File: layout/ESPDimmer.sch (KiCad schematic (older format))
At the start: 11 parts, among them P1 CONN_01X03, P2 Serial, P3 LED, P4 ProgMod, P5 DS18B20, Q1 Q_NMOS_GDS, U1 LD1117S33CTR, U2 ESP-12E

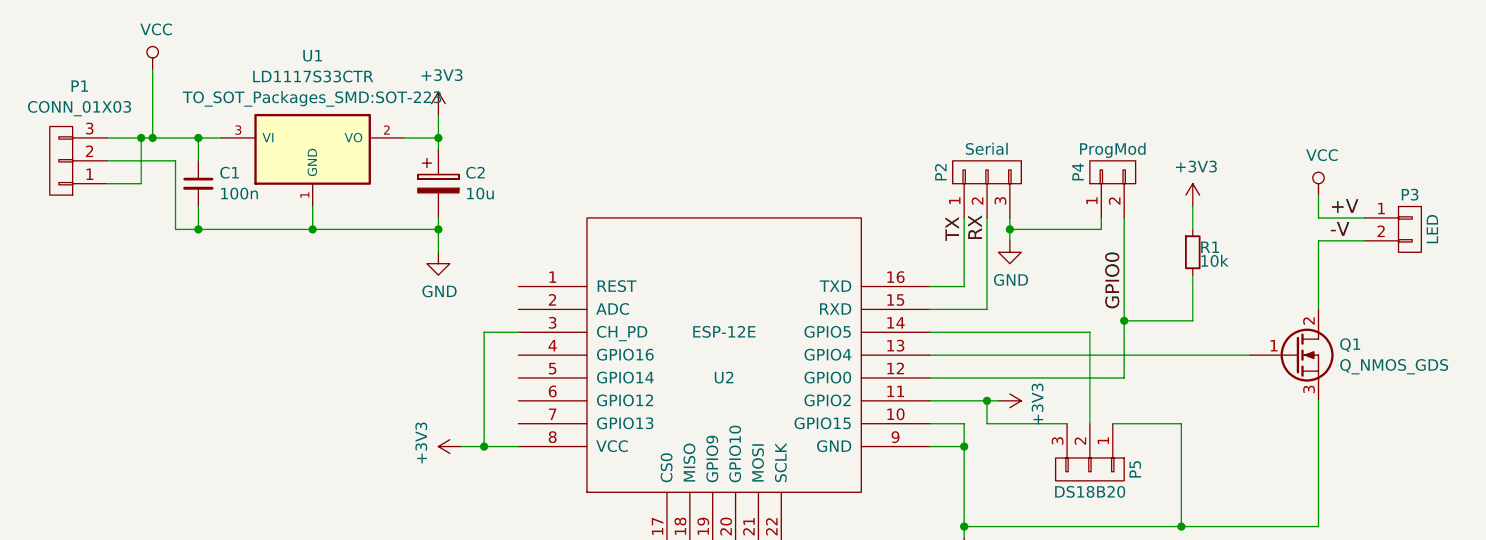
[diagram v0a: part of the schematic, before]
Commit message: Updated part names and corrected the power supply traces that were shorted!
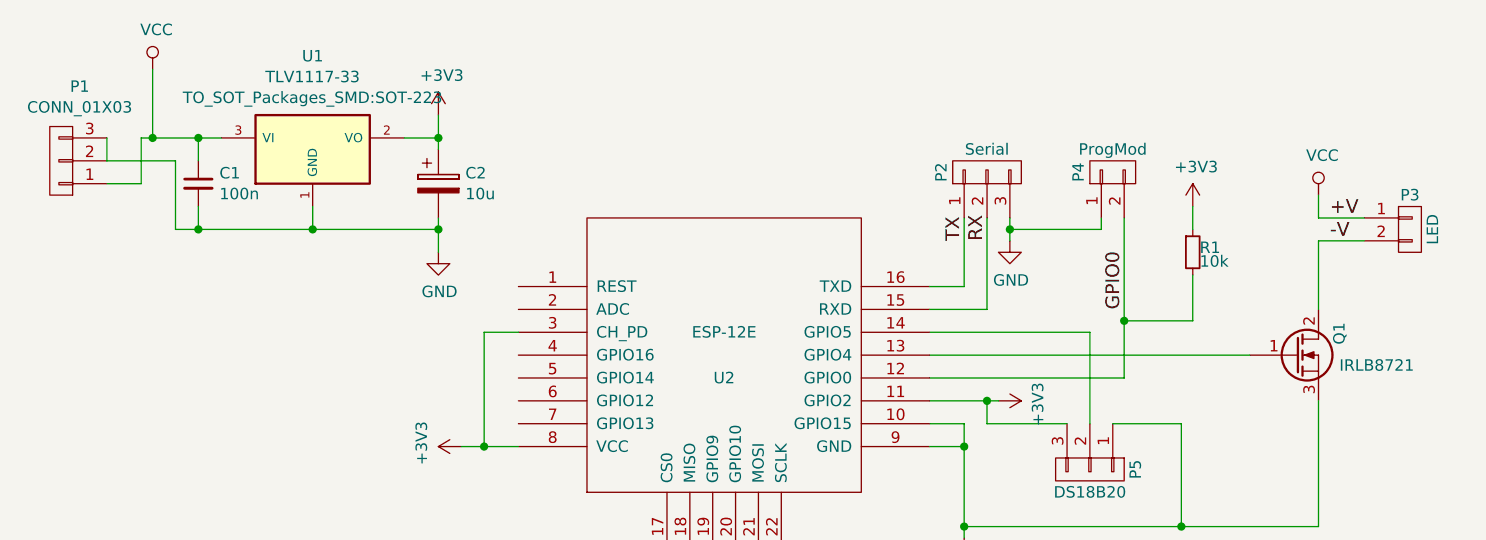
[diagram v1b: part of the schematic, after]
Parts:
- C2: footprint Capacitors_SMD:C_0402 -> Capacitors_SMD:C_0603
- Q1: value Q_NMOS_GDS -> IRLB8721
- U1: value LD1117S33CTR -> TLV1117-33
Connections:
- net GND: now also P1.3 (P3)
- net VCC: no longer P1.3 (P3)
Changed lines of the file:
@@
 P 3150 1800
 F 0 "U1" H 3150 2208 50  0000 C CNN
-F 1 "LD1117S33CTR" H 3150 2117 50  0000 C CNN
+F 1 "TLV1117-33" H 3150 2117 50  0000 C CNN
 F 2 "TO_SOT_Packages_SMD:SOT-223" H 3150 2026 50  0000 C CNN
 F 3 "" H 3150 1800 50  0000 C CNN
@@
 $EndComp
 Wire Wire Line
-	2250 1750 2750 1750
-Wire Wire Line
 	2250 1850 2550 1850
 Wire Wire Line
@@
 Wire Wire Line
 	2400 1950 2400 1750
-Connection ~ 2400 1750
 $Comp
 L CP C2
@@
 F 0 "C2" H 3818 1996 50  0000 L CNN
 F 1 "10u" H 3818 1905 50  0000 L CNN
-F 2 "Capacitors_SMD:C_0402" H 3738 1800 50  0001 C CNN
+F 2 "Capacitors_SMD:C_0603" H 3738 1800 50  0001 C CNN
 F 3 "" H 3700 1950 50  0000 C CNN
 	1    3700 1950
@@
 $EndComp
 Wire Wire Line
-	2650 1850 2650 1750
+	2650 1750 2650 1850
 Connection ~ 2650 1750
 Wire Wire Line
@@
 U 1 1 58663ECC
 P 7450 2700
-F 0 "Q1" H 7641 2746 50  0000 L CNN
-F 1 "Q_NMOS_GDS" H 7641 2655 50  0000 L CNN
+F 0 "Q1" V 7641 2746 50  0000 L CNN
+F 1 "IRLB8721" H 7641 2655 50  0000 L CNN
 F 2 "TO_SOT_Packages_THT:TO-220_Neutral123_Vertical" H 7650 2800 50  0001 C CNN
 F 3 "" H 7450 2700 50  0000 C CNN
@@
 	6100 3000 6100 2900
 Connection ~ 6100 2900
+Wire Wire Line
+	2400 1750 2750 1750
+Wire Wire Line
+	2250 1750 2250 1850
 $EndSCHEMATC

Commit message: Updated capacitors and other small changes
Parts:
- removed C2: 10u, Capacitors_SMD:C_0603, symbol CP
- added C2: 100n, Capacitors_SMD:C_0402, symbol C_Small
- added C3: 1u, Capacitors_SMD:C_0402, symbol C_Small
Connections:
- net +3V3: now also C2.1, C3.1
- net GND: now also C2.2, C3.2
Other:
- moved on the sheet: C1, P1, U1
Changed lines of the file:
@@
 L LD1117S33CTR U1
 U 1 1 57E69AF7
-P 3150 1800
-F 0 "U1" H 3150 2208 50  0000 C CNN
-F 1 "TLV1117-33" H 3150 2117 50  0000 C CNN
-F 2 "TO_SOT_Packages_SMD:SOT-223" H 3150 2026 50  0000 C CNN
-F 3 "" H 3150 1800 50  0000 C CNN
-	1    3150 1800
+P 3100 6200
+F 0 "U1" H 3100 6608 50  0000 C CNN
+F 1 "TLV1117-33" H 3100 6517 50  0000 C CNN
+F 2 "TO_SOT_Packages_SMD:SOT-223" H 3100 6426 50  0000 C CNN
+F 3 "" H 3100 6200 50  0000 C CNN
+	1    3100 6200
 	1    0    0    -1
 $EndComp
@@
 L CONN_01X03 P1
 U 1 1 57E69B46
-P 2050 1850
-F 0 "P1" H 1969 1525 50  0000 C CNN
-F 1 "CONN_01X03" H 1969 1616 50  0000 C CNN
-F 2 "Connect:BARREL_JACK" H 2050 1850 50  0001 C CNN
-F 3 "" H 2050 1850 50  0000 C CNN
-	1    2050 1850
+P 2000 6250
+F 0 "P1" H 1919 5925 50  0000 C CNN
+F 1 "CONN_01X03" H 1919 6016 50  0000 C CNN
+F 2 "Connect:BARREL_JACK" H 2000 6250 50  0001 C CNN
+F 3 "" H 2000 6250 50  0000 C CNN
+	1    2000 6250
 	-1   0    0    1
 $EndComp
 Wire Wire Line
-	2250 1850 2550 1850
-Wire Wire Line
-	2550 1850 2550 2150
-Wire Wire Line
-	2550 2150 3700 2150
-Wire Wire Line
-	3150 2150 3150 2050
-Wire Wire Line
-	2250 1950 2400 1950
-Wire Wire Line
-	2400 1950 2400 1750
-$Comp
-L CP C2
-U 1 1 57E69BD2
-P 3700 1950
-F 0 "C2" H 3818 1996 50  0000 L CNN
-F 1 "10u" H 3818 1905 50  0000 L CNN
-F 2 "Capacitors_SMD:C_0603" H 3738 1800 50  0001 C CNN
-F 3 "" H 3700 1950 50  0000 C CNN
-	1    3700 1950
-	1    0    0    -1
-$EndComp
+	2200 6250 2500 6250
+Wire Wire Line
+	2500 6250 2500 6550
+Wire Wire Line
+	2500 6550 3900 6550
+Wire Wire Line
+	3100 6550 3100 6450
+Wire Wire Line
+	2200 6350 2350 6350
+Wire Wire Line
+	2350 6350 2350 6150
 $Comp
 L C_Small C1
 U 1 1 57E69BFC
-P 2650 1950
-F 0 "C1" H 2742 1996 50  0000 L CNN
-F 1 "100n" H 2742 1905 50  0000 L CNN
-F 2 "Capacitors_SMD:C_0402" H 2650 1950 50  0001 C CNN
-F 3 "" H 2650 1950 50  0000 C CNN
-	1    2650 1950
-	1    0    0    -1
-$EndComp
-Wire Wire Line
-	2650 1750 2650 1850
-Connection ~ 2650 1750
-Wire Wire Line
-	2650 2050 2650 2150
-Connection ~ 2650 2150
-Wire Wire Line
-	3700 2100 3700 2250
-Connection ~ 3150 2150
-Wire Wire Line
-	3550 1750 3700 1750
-Wire Wire Line
-	3700 1650 3700 1800
+P 2600 6350
+F 0 "C1" H 2692 6396 50  0000 L CNN
+F 1 "100n" H 2692 6305 50  0000 L CNN
+F 2 "Capacitors_SMD:C_0402" H 2600 6350 50  0001 C CNN
+F 3 "" H 2600 6350 50  0000 C CNN
+	1    2600 6350
+	1    0    0    -1
+$EndComp
+Wire Wire Line
+	2600 6150 2600 6250
+Connection ~ 2600 6150
+Wire Wire Line
+	2600 6450 2600 6550
+Connection ~ 2600 6550
+Wire Wire Line
+	3650 6400 3650 6650
+Connection ~ 3100 6550
+Wire Wire Line
+	3500 6150 3900 6150
+Wire Wire Line
+	3650 6050 3650 6200
 $Comp
 L GND #PWR01
 U 1 1 57E69D04
-P 3700 2250
-F 0 "#PWR01" H 3700 2000 50  0001 C CNN
-F 1 "GND" H 3705 2077 50  0000 C CNN
-F 2 "" H 3700 2250 50  0000 C CNN
-F 3 "" H 3700 2250 50  0000 C CNN
-	1    3700 2250
-	1    0    0    -1
-$EndComp
-Connection ~ 3700 1750
-Connection ~ 3700 2150
+P 3650 6650
+F 0 "#PWR01" H 3650 6400 50  0001 C CNN
+F 1 "GND" H 3655 6477 50  0000 C CNN
+F 2 "" H 3650 6650 50  0000 C CNN
+F 3 "" H 3650 6650 50  0000 C CNN
+	1    3650 6650
+	1    0    0    -1
+$EndComp
+Connection ~ 3650 6150
+Connection ~ 3650 6550
 $Comp
 L GND #PWR02
@@
 L +3V3 #PWR03
 U 1 1 586638C3
-P 3700 1650
-F 0 "#PWR03" H 3700 1500 50  0001 C CNN
-F 1 "+3V3" H 3715 1823 50  0000 C CNN
-F 2 "" H 3700 1650 50  0000 C CNN
-F 3 "" H 3700 1650 50  0000 C CNN
-	1    3700 1650
+P 3650 6050
+F 0 "#PWR03" H 3650 5900 50  0001 C CNN
+F 1 "+3V3" H 3665 6223 50  0000 C CNN
+F 2 "" H 3650 6050 50  0000 C CNN
+F 3 "" H 3650 6050 50  0000 C CNN
+	1    3650 6050
 	1    0    0    -1
 $EndComp
@@
 L VCC #PWR04
 U 1 1 586639B4
-P 2450 1450
-F 0 "#PWR04" H 2450 1300 50  0001 C CNN
-F 1 "VCC" H 2467 1623 50  0000 C CNN
-F 2 "" H 2450 1450 50  0000 C CNN
-F 3 "" H 2450 1450 50  0000 C CNN
-	1    2450 1450
-	1    0    0    -1
-$EndComp
-Wire Wire Line
-	2450 1450 2450 1750
-Connection ~ 2450 1750
+P 2400 5850
+F 0 "#PWR04" H 2400 5700 50  0001 C CNN
+F 1 "VCC" H 2417 6023 50  0000 C CNN
+F 2 "" H 2400 5850 50  0000 C CNN
+F 3 "" H 2400 5850 50  0000 C CNN
+	1    2400 5850
+	1    0    0    -1
+$EndComp
+Wire Wire Line
+	2400 5850 2400 6150
+Connection ~ 2400 6150
 $Comp
 L Q_NMOS_GDS Q1
@@
 Connection ~ 6100 2900
 Wire Wire Line
-	2400 1750 2750 1750
-Wire Wire Line
-	2250 1750 2250 1850
+	2350 6150 2700 6150
+Wire Wire Line
+	2200 6150 2200 6250
+$Comp
+L C_Small C2
+U 1 1 58668A1E
+P 3650 6300
+F 0 "C2" H 3742 6346 50  0000 L CNN
+F 1 "100n" H 3742 6255 50  0000 L CNN
+F 2 "Capacitors_SMD:C_0402" H 3650 6300 50  0001 C CNN
+F 3 "" H 3650 6300 50  0000 C CNN
+	1    3650 6300
+	1    0    0    -1
+$EndComp
+$Comp
+L C_Small C3
+U 1 1 58668A66
+P 3900 6300
+F 0 "C3" H 3992 6346 50  0000 L CNN
+F 1 "1u" H 3992 6255 50  0000 L CNN
+F 2 "Capacitors_SMD:C_0402" H 3900 6300 50  0001 C CNN
+F 3 "" H 3900 6300 50  0000 C CNN
+	1    3900 6300
+	1    0    0    -1
+$EndComp
+Wire Wire Line
+	3900 6150 3900 6200
+Wire Wire Line
+	3900 6550 3900 6400
 $EndSCHEMATC

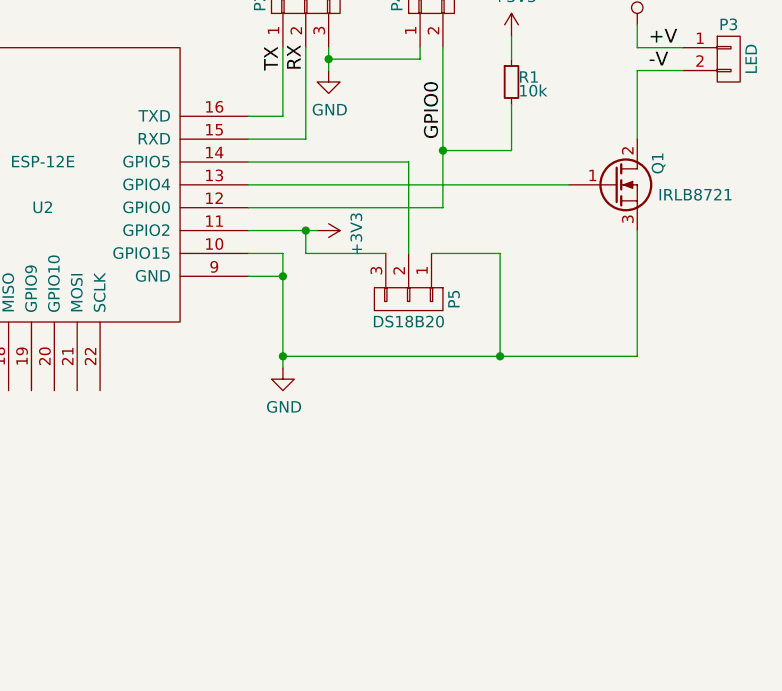
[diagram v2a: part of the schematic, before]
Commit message: Added pull-up resistor needed for the OneWire communication with the DS18B20 thermometer.
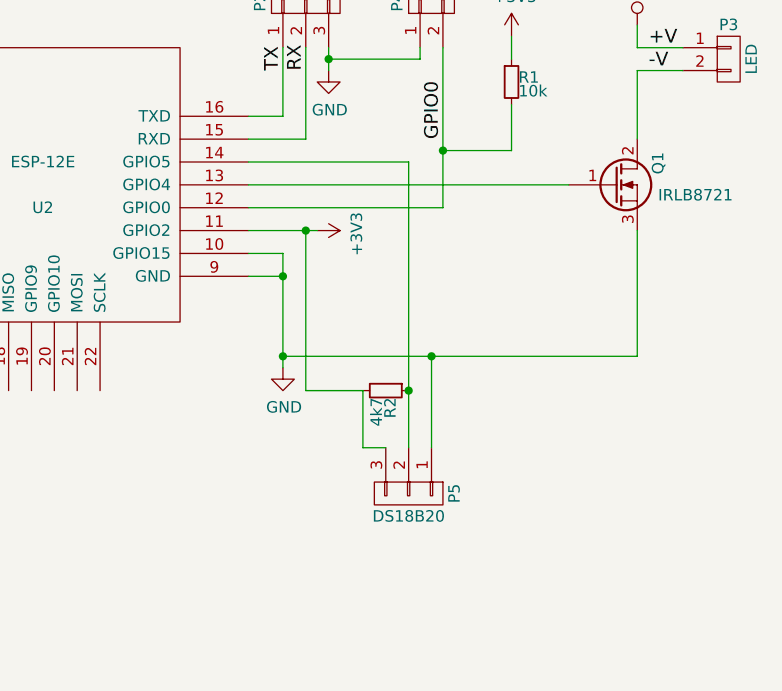
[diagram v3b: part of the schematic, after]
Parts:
- added R2: 4k7, Resistors_SMD:R_0805, symbol R_Small
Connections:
- net +3V3: now also R2.2
- net at P5.2 (P2), U2.14 (GPIO5): now also R2.1
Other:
- moved on the sheet: P5
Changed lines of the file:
@@
 L CONN_01X03 P5
 U 1 1 5866589E
-P 6550 3200
-F 0 "P5" H 6550 3400 50  0000 C CNN
-F 1 "DS18B20" V 6650 3200 50  0000 C CNN
-F 2 "TO_SOT_Packages_THT:TO-92_Inline_Narrow_Oval" H 6550 3200 50  0001 C CNN
-F 3 "" H 6550 3200 50  0000 C CNN
-	1    6550 3200
+P 6550 4050
+F 0 "P5" H 6550 4250 50  0000 C CNN
+F 1 "DS18B20" V 6650 4050 50  0000 C CNN
+F 2 "TO_SOT_Packages_THT:TO-92_Inline_Narrow_Oval" H 6550 4050 50  0001 C CNN
+F 3 "" H 6550 4050 50  0000 C CNN
+	1    6550 4050
 	0    1    1    0
 $EndComp
@@
 	5850 2600 6550 2600
 Wire Wire Line
-	6550 2600 6550 3000
+	6550 2600 6550 3850
 Wire Wire Line
-	6650 3000 6950 3000
-Wire Wire Line
-	6950 3000 6950 3450
-Connection ~ 6950 3450
-Wire Wire Line
-	6450 3000 6100 3000
-Wire Wire Line
-	6100 3000 6100 2900
+	6100 2900 6100 3600
 Connection ~ 6100 2900
 Wire Wire Line
@@
 Wire Wire Line
 	3900 6550 3900 6400
+$Comp
+L R_Small R2
+U 1 1 58678B77
+P 6450 3600
+F 0 "R2" H 6480 3620 50  0000 L CNN
+F 1 "4k7" H 6480 3560 50  0000 L CNN
+F 2 "Resistors_SMD:R_0805" H 6450 3600 50  0001 C CNN
+F 3 "" H 6450 3600 50  0000 C CNN
+	1    6450 3600
+	0    1    1    0
+$EndComp
+Wire Wire Line
+	6100 3600 6350 3600
+Wire Wire Line
+	6350 3600 6350 3850
+Wire Wire Line
+	6350 3850 6450 3850
+Connection ~ 6550 3600
+Wire Wire Line
+	6650 3850 6650 3450
+Connection ~ 6650 3450
 $EndSCHEMATC
